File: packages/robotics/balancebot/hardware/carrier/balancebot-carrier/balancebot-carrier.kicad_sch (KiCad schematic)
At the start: 22 parts, among them J1 JST-XH pack in, J2 LM2596 module, J3 GY-521 MPU6050, J4 Motor left, J5 Motor right, Q1 ZXMP4A16G, U1 XIAO RP2350

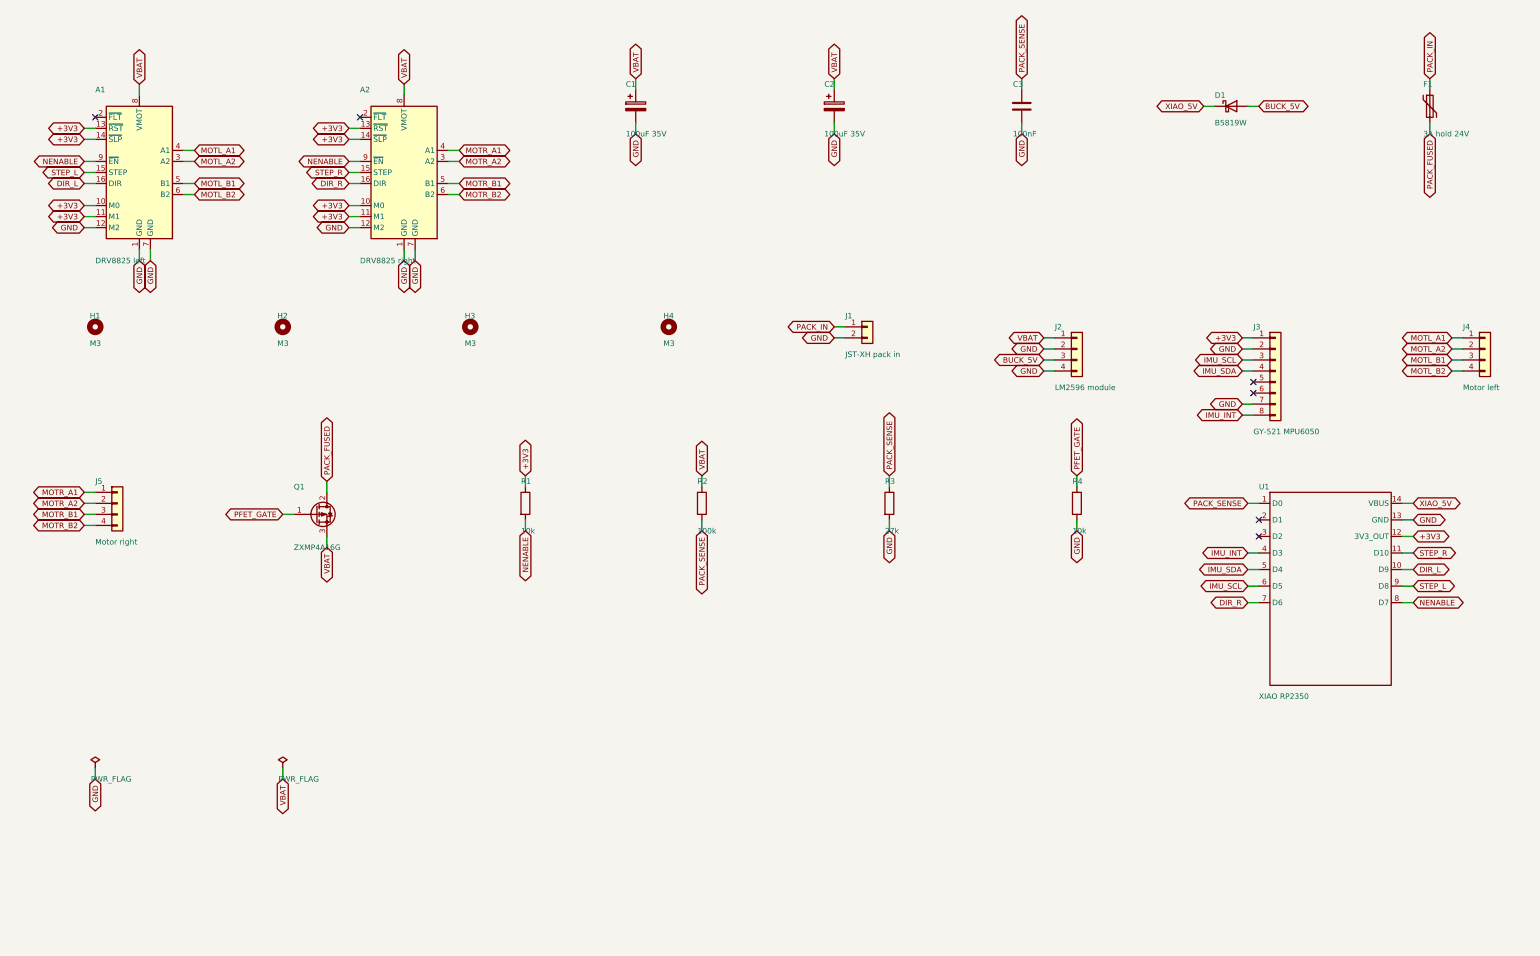
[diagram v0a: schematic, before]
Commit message: fix(balancebot): clamp Q1's gate with a 15 V zener
The pack-input text justified F1's 24 V rating by a hot-plug overshoot
above the 12.6 V pack, yet ruled out a gate zener because |VGS| reaches
only 12.6 V. The same overshoot lands on Q1's source while R4 holds the
gate at GND, so above 20 V it exceeds the ZXMP4A16G's VGSS (DS33584).

D2, a BZT52C15 (VZ 13.8-15.6 V at 5 mA, JSCJ Rev. 2.1), goes from Q1's
source (cathode) to its gate (anode); R4 limits its current. Its minimum
is above a full pack, so in use |VGS| still follows the pack (8.2-12.6 V,
past the -4.5 V the 100 mohm RDS(on) maximum is rated at), and in an
overshoot it holds |VGS| at or under 15.6 V (about 16.9 V at 125 C).

On the board D2 sits east of Q1's pins with all of PFET_GATE and its
cathode tie as fixed tracks: with only the anode tie fixed, its keepout
boxed in R4's gate pad and Freerouting left PFET_GATE unrouted on every
run. R4 moves down 0.5 mm and its reference beside it. The perfboard
gains a 1N4744A above Q1.

The README now gives a labelled hot-plug inrush estimate (about 30 A
peak, 80 us, above ISM's 21 A for about 30 us, no limiter), and the
Q1-to-A2 VBAT length as measured: 130.8 mm of track centreline; the
earlier 129 mm came from a path sum that skipped a 1.3 mm corner.

Co-Authored-By: Claude Opus 5.5 <noreply@anthropic.com>
Claude-Session: https://claude.ai/code/session_01DgeoMcrSCUfJwedu77q6oo
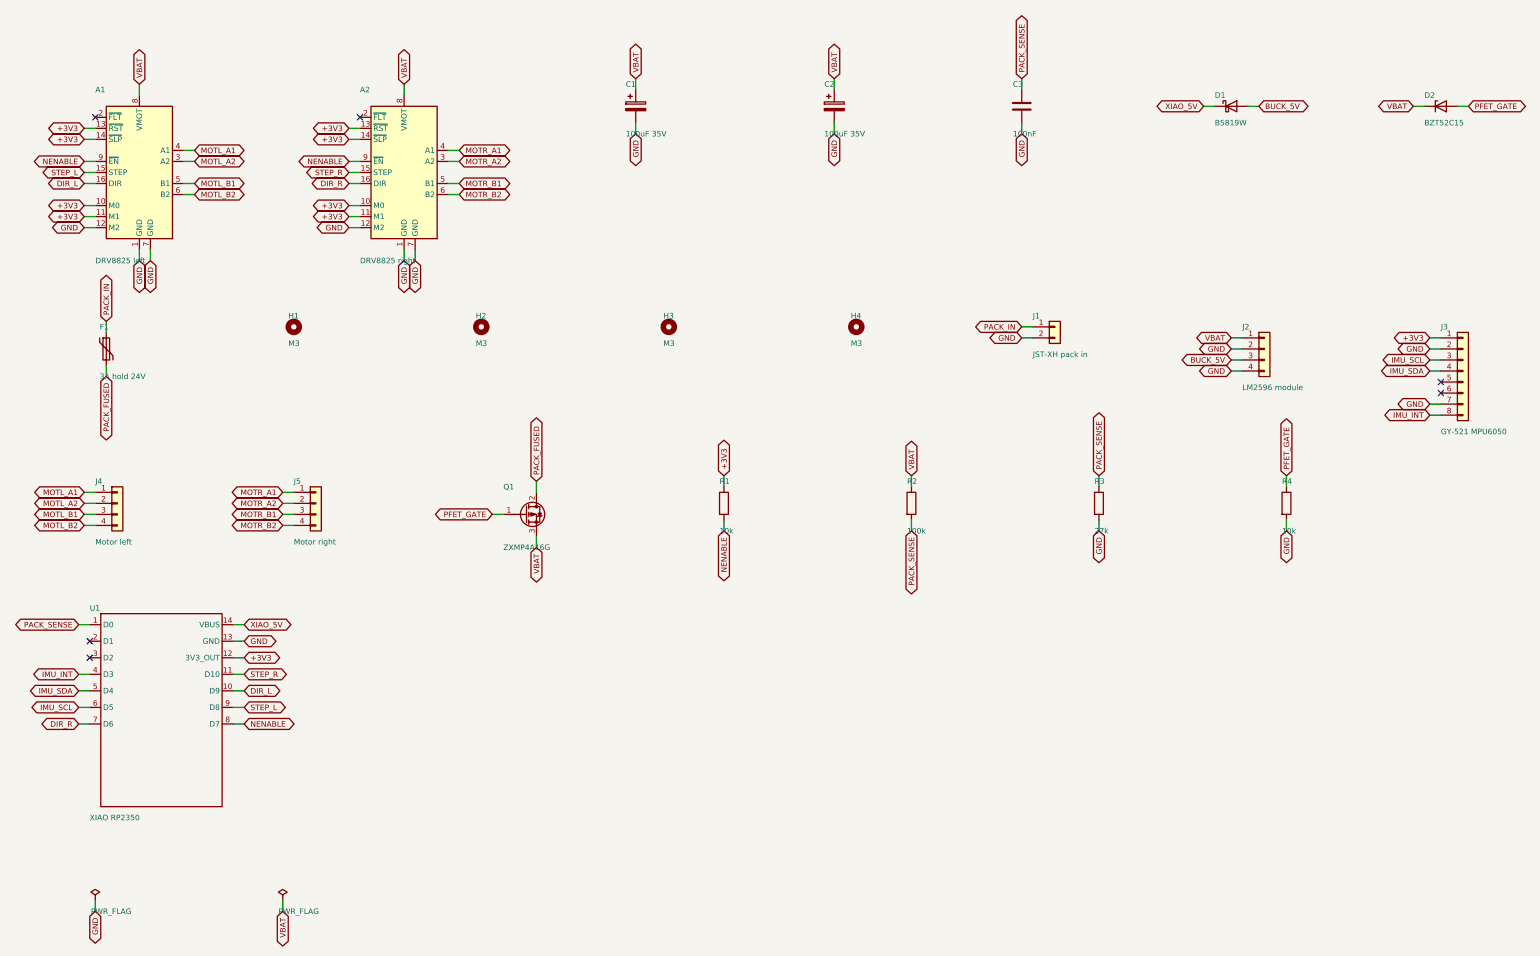
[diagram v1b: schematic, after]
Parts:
- added D2: BZT52C15, Diode_SMD:D_SOD-123, symbol Device:D_Zener
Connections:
- net PFET_GATE: now also D2.2 (A)
- net VBAT: now also D2.1 (K)
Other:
- moved on the sheet: F1, H1, H2, H3, H4, J1, J2, J3, J4, J5, Q1, R1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
